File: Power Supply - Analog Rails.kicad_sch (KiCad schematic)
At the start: 30 parts, among them IC3 LTC6655BHMS8-2.5#PBF, IC5 LT8362EMSE#PBF, IC7 LTC6655BHMS8-5#PBF, IC8 LT3045EDD-1#TRPBF, IC9 LT3045EDD-1#TRPBF

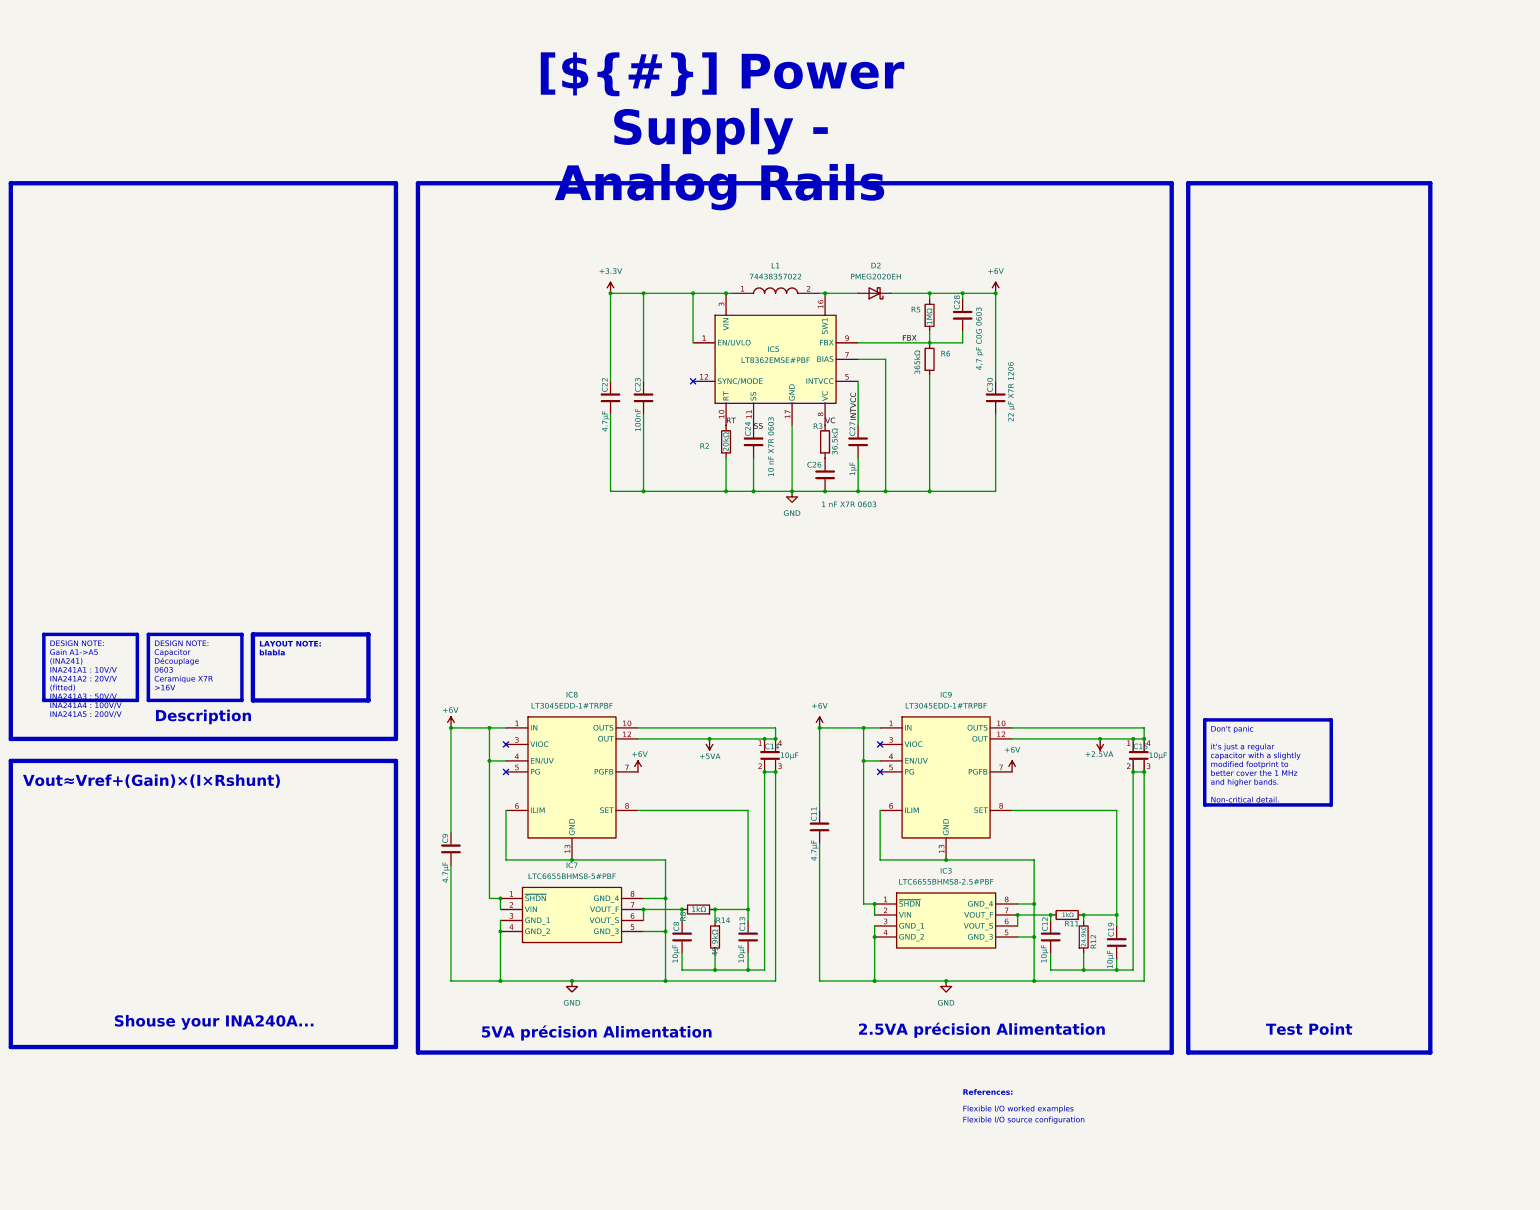
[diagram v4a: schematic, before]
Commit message: Restyle schematic sheets, new title block logo, WE-MAPI inductor in simulations
- Schematic sheets: restyled frames, tables and text boxes
- Title block: INGENIERIE FRANCE logo in KDT_Template_GIT.kicad_wks
- LTspice: L1 modelled as WE-MAPI 4030 74438357022 (22 mOhm),
  simulations 01 and 03 rerun, README and results updated

Co-Authored-By: Claude Opus 5.5 <noreply@anthropic.com>
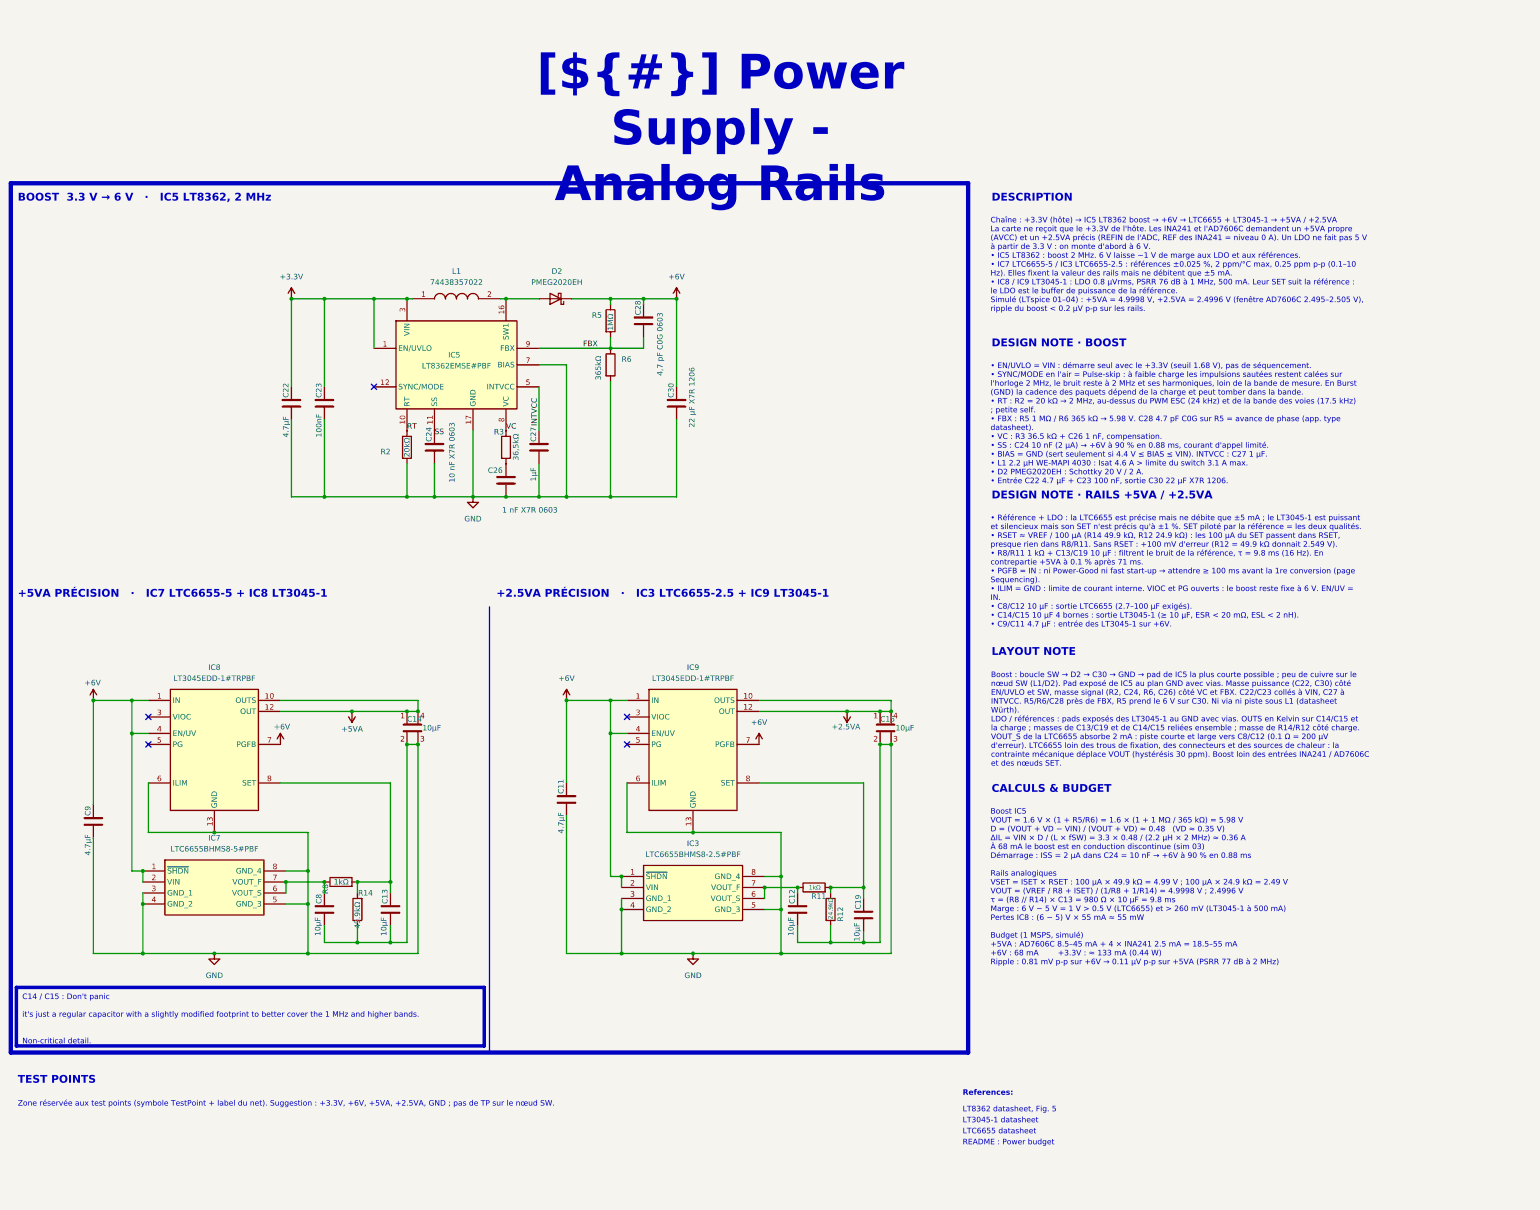
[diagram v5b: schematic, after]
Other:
- note added: "LT3045-1 datasheet"
- note added: "LT8362 datasheet, Fig. 5"
- note added: "LTC6655 datasheet"
- note added: "README : Power budget"
- note removed: "Flexible I/O source configuration"
- note removed: "Flexible I/O worked examples"
- note removed: "Vout≈Vref+(Gain)×(I×Rshunt)"
- moved on the sheet: C11, C12, C13, C14, C15, C19, C22, C23, C24, C26, C27, C28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

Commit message: Wire the AD7606C-18 digital side to host header J4, add test points
- AD7606C-18: software mode (OS0-2 high), serial (PAR/SER SEL high),
  REF SELECT low; CONVST, BUSY, RESET, CS, SCLK, SDI, FRSTDATA and
  DOUTA-D to J4 (2x8 pin header 2.54 mm, horizontal), +3.3V on J4 pin 1
- AD7606C-18 AGND pin 26 and REFGND pin 46 on GND
- Test points TP1-TP16: rails, INA241 outputs, CONVST, BUSY
- Nets renamed SHUNT_*, INA_*, ADC_*; net colours in the project
- LT3045-1 footprint: thermal vias numbered as exposed pad 13
- PCB updated from the schematic; ADC_* digital nets not routed yet
- README template / CHANGELOG: status, J4 pinout, design review 1 and 2
  fixed, new finding 9 (VDRIVE above AVCC + 0.3 V at power-up),
  4 channels / 8 ADC inputs

Co-Authored-By: Claude Opus 5.5 <noreply@anthropic.com>
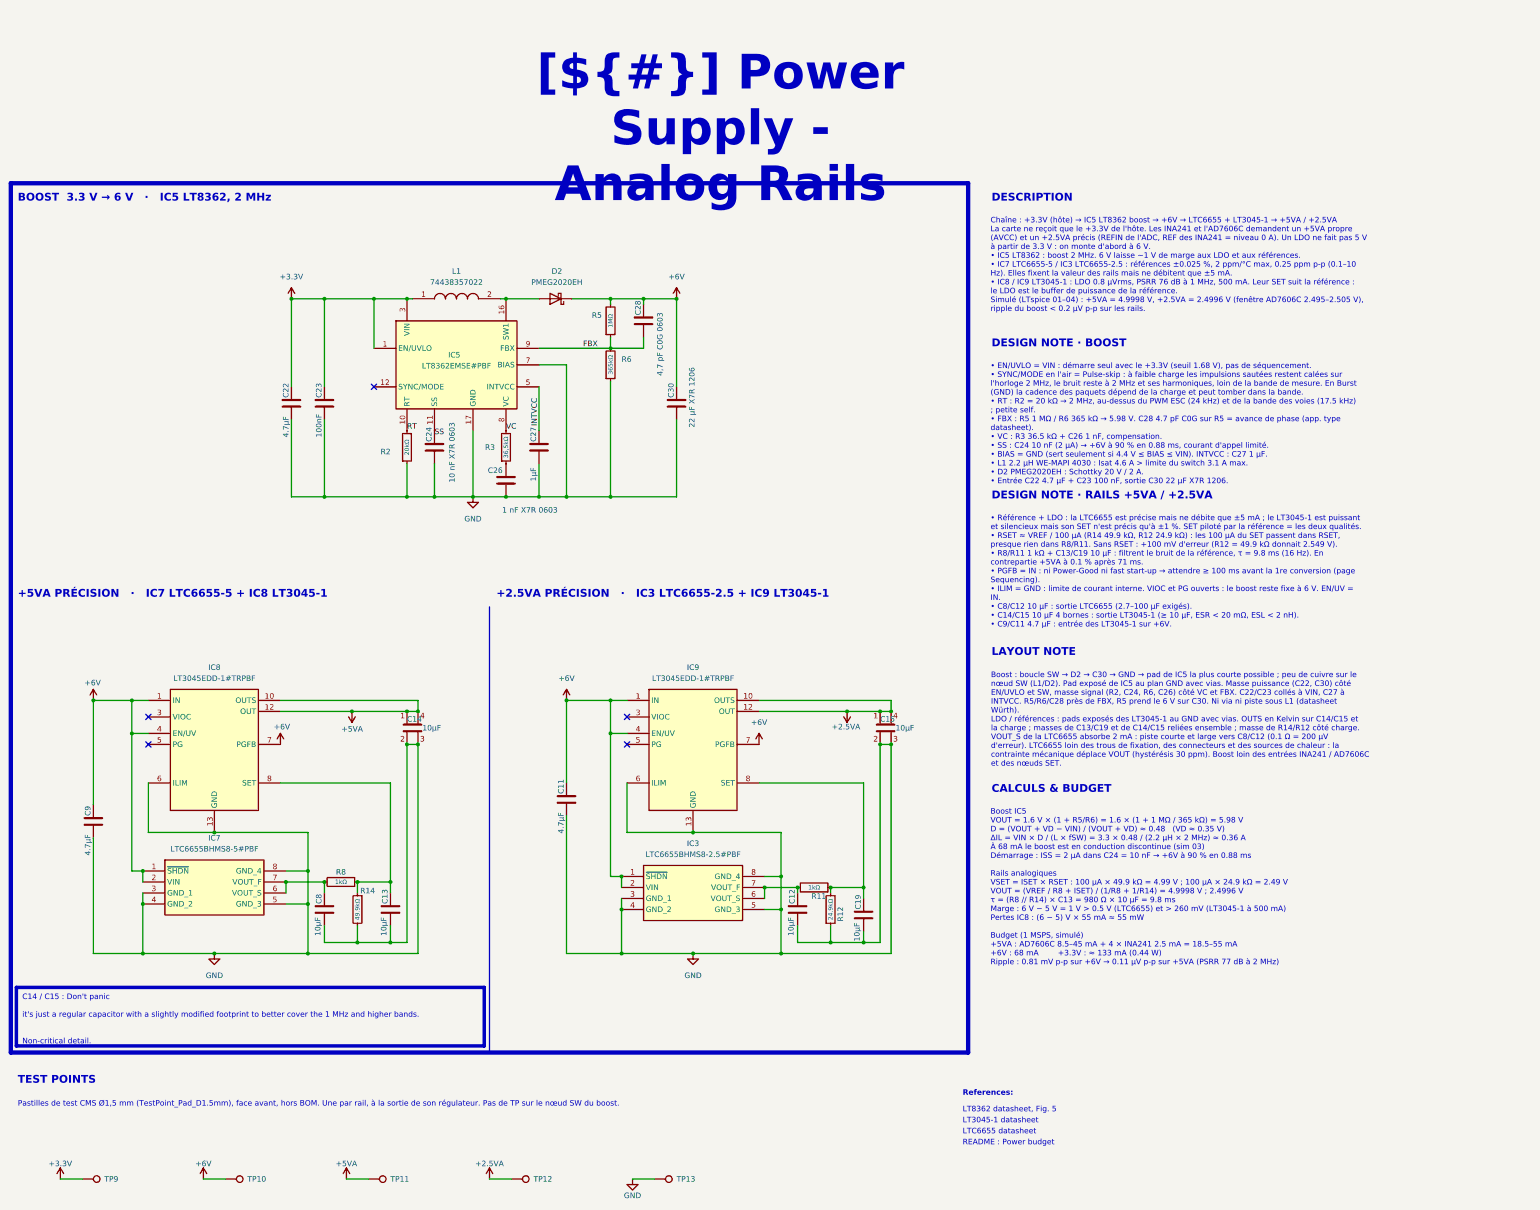
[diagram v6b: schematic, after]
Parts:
- added TP10, TP11, TP12, TP13, TP9: TestPoint, OPEN_PHASE:TestPoint_Pad_D1.5mm, symbol OPEN_PHASE:TestPoint
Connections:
- net +2.5VA: now also TP12.1
- net +3.3V: now also TP9.1
- net +5VA: now also TP11.1
- net +6V: now also TP10.1
- net GND: now also TP13.1
